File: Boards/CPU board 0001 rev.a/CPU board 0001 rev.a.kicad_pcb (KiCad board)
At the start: 2 copper layers, 165.9 x 187.4 mm, 78 parts, among them J1 CEC card edge connector large, U1 SPARE, U10 7432, U11 7442, U12 7406, U13 7406, U14 7442, U15 7442, U16 M8216, U17 M8216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

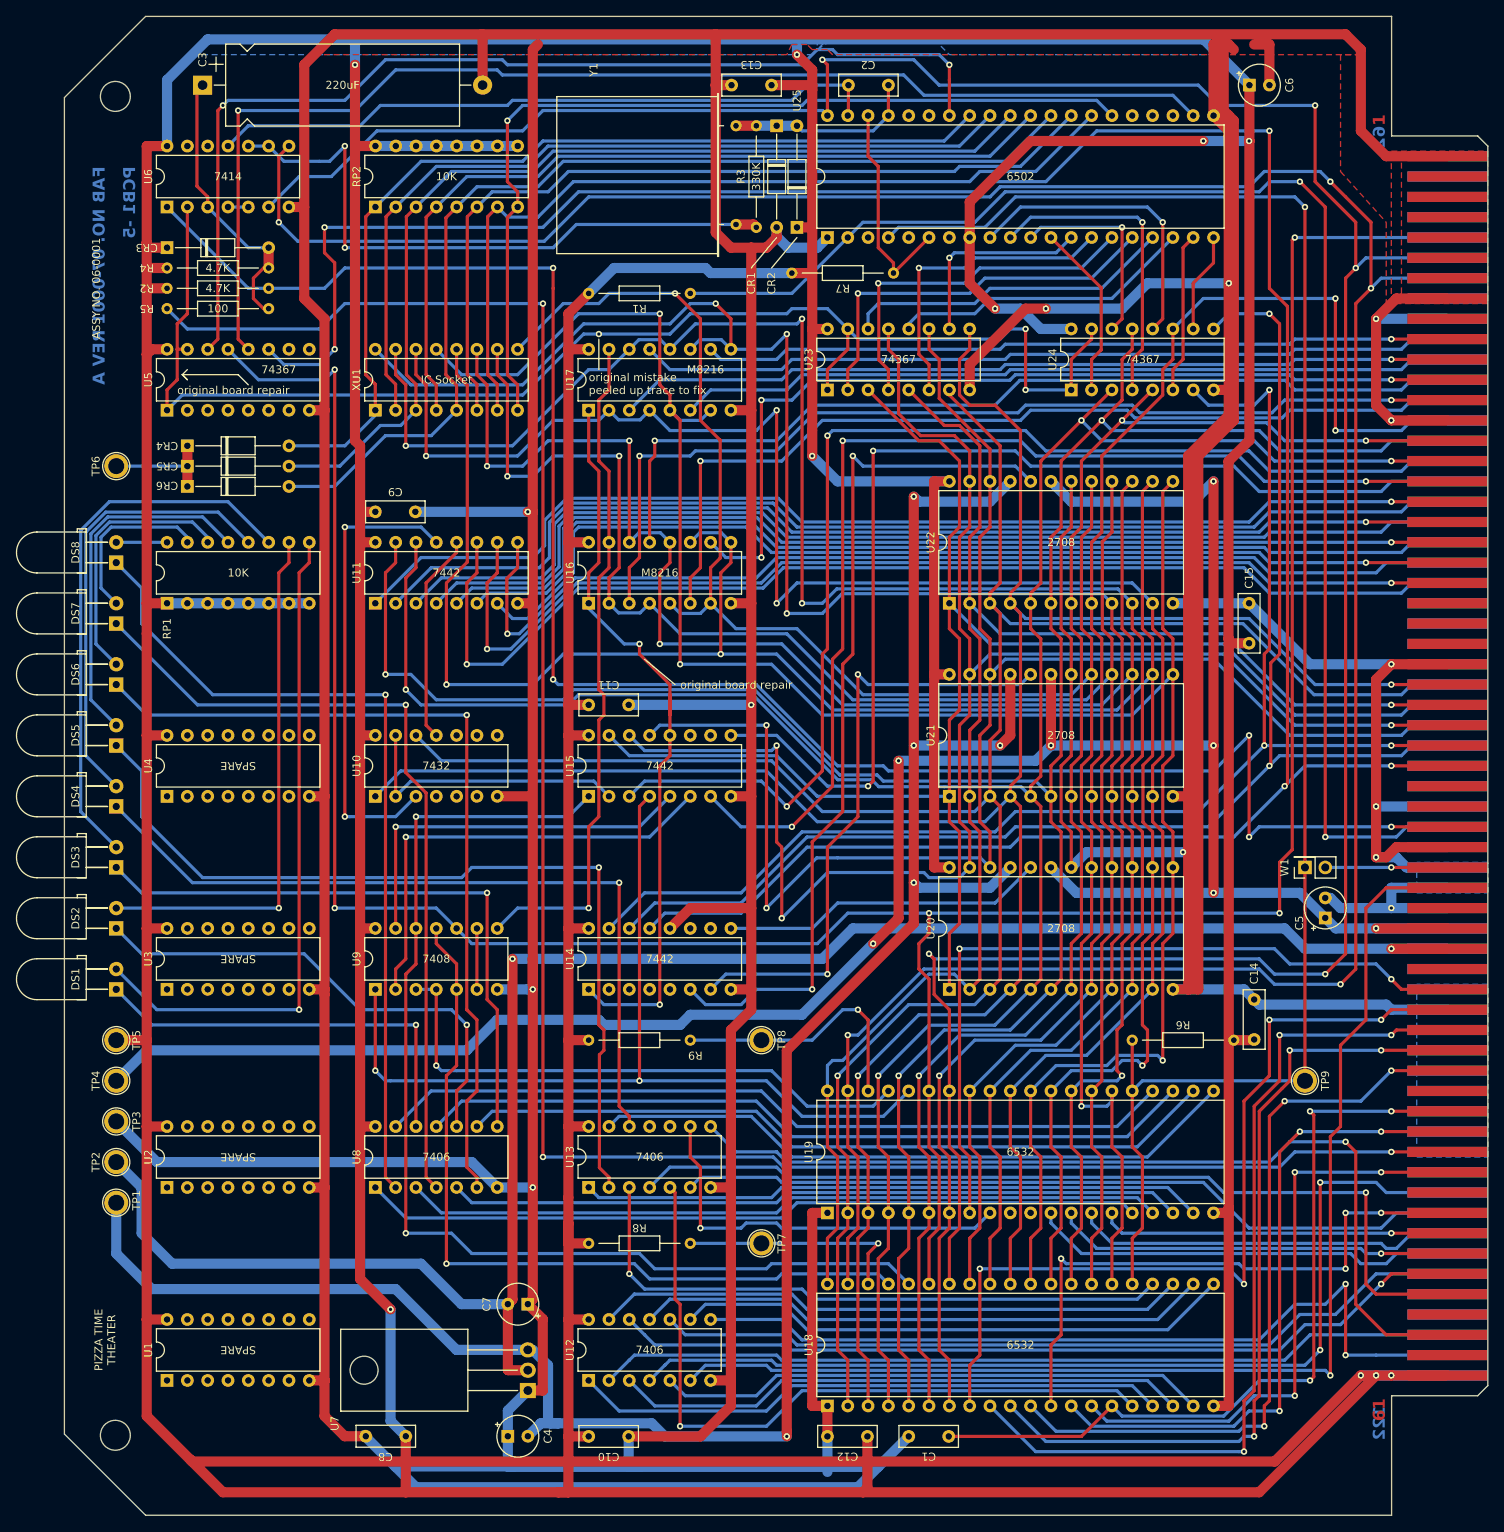
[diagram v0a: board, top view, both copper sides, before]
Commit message: updated boards per real one
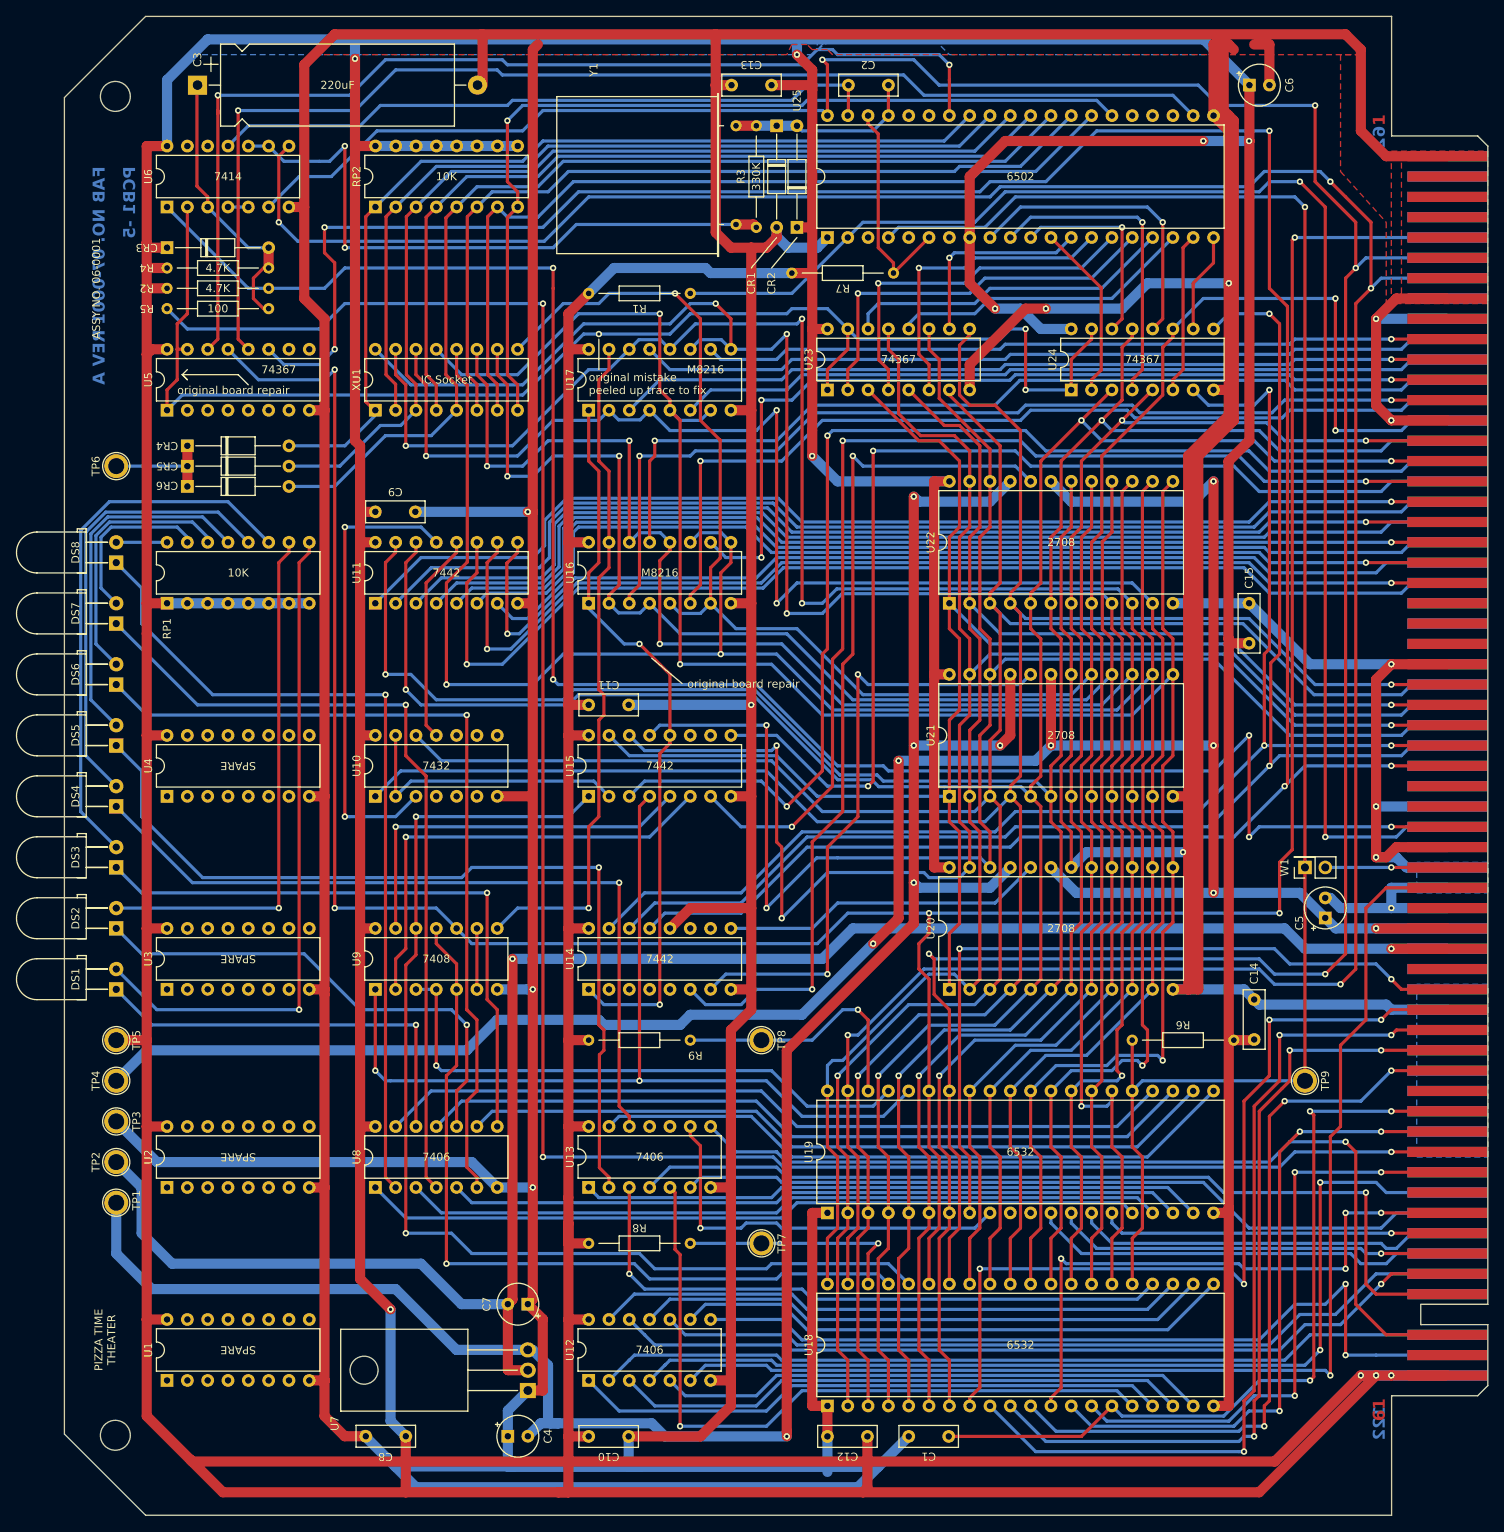
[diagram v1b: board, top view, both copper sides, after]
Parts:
- moved C3 0.63 mm to (58.4, 19.1)
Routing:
- net Net-(U14-0): track 93.4 -> 90.9 mm
- net +5V: track 1497.0 -> 1498.9 mm
- net cpu R/~{W}: track 132.6 -> 134.1 mm
- net Net-(CR3-A): track 35.8 -> 34.8 mm

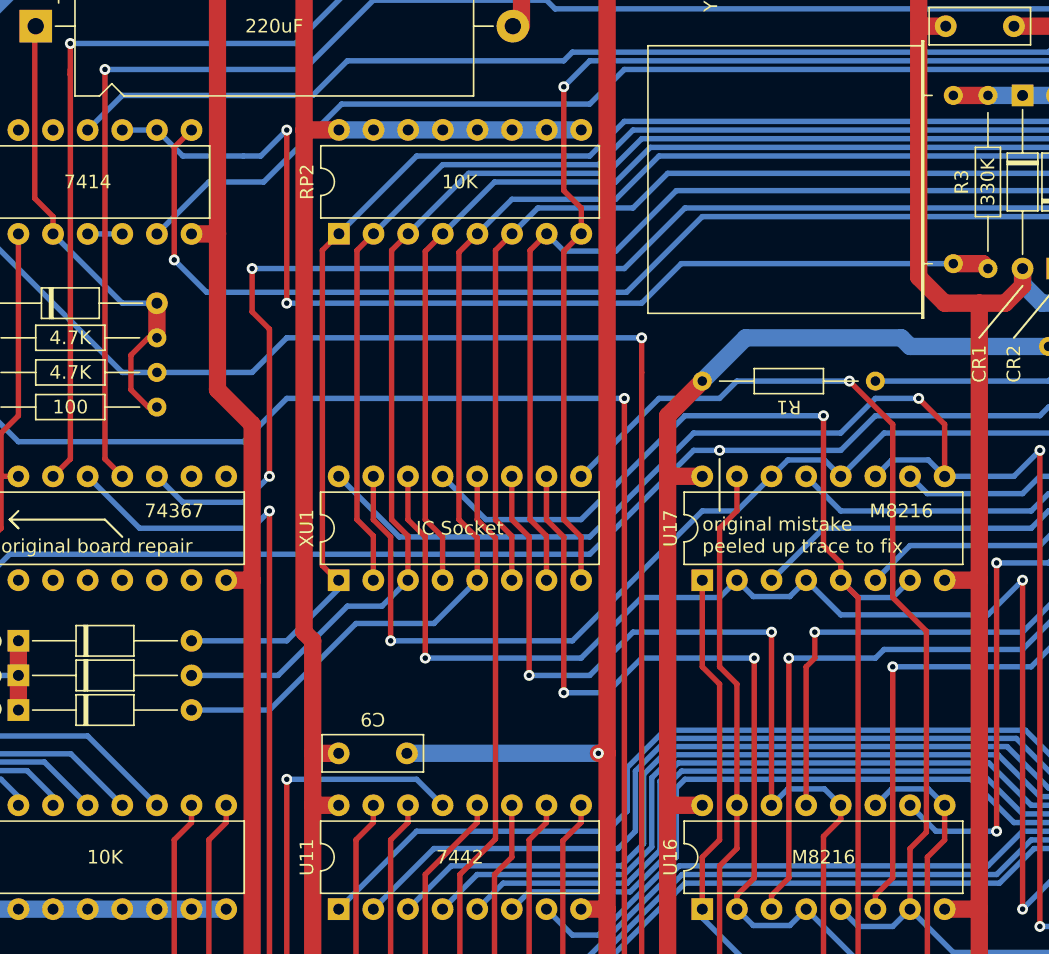
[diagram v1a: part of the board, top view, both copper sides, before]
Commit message: revisions from real life boards
tip130a is actually tip30a, widened holes for crystal, widened holes for big power resistor, fixed cpu board LED resistors
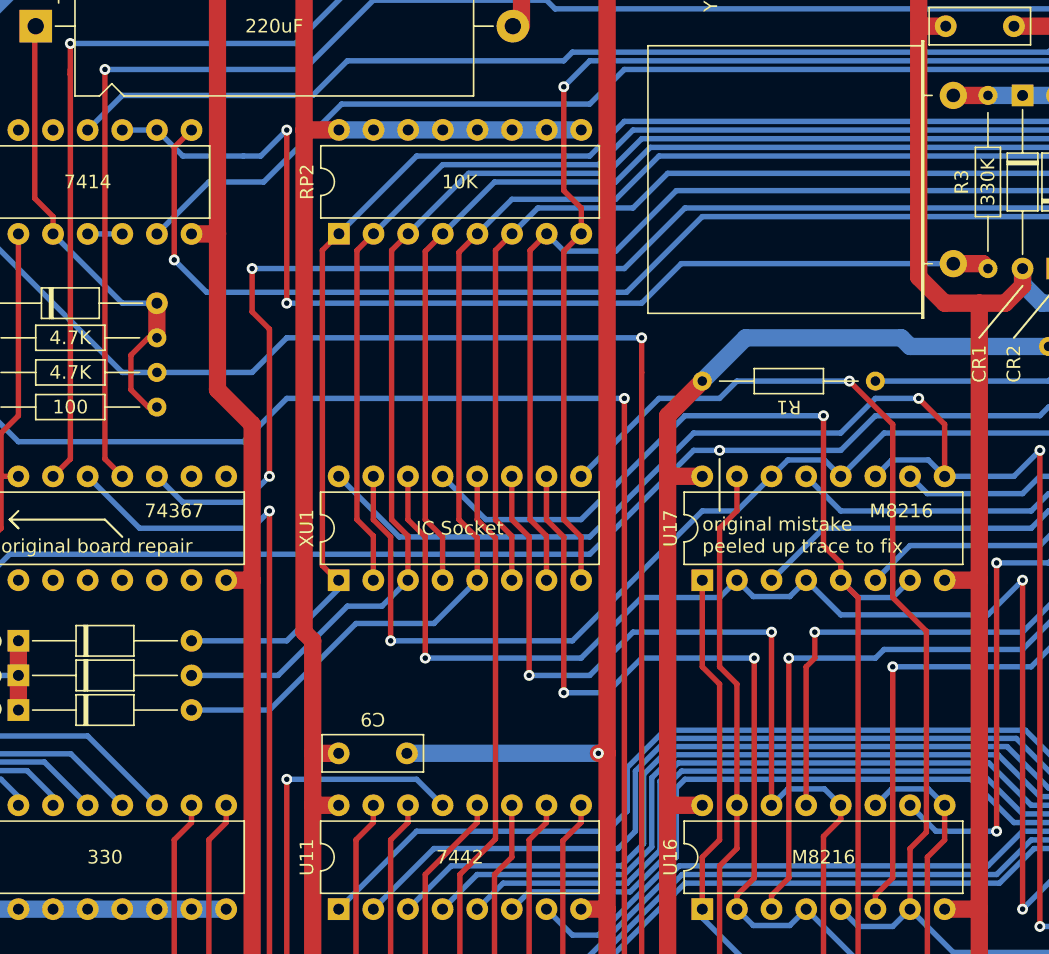
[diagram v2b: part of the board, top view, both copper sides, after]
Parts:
- RP1: value 10K -> 330
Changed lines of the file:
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@@
         (effects (font (size 1 1) (thickness 0.15)))
     )
-    (fp_text value "10K" (at 3.81 8.89 180) (layer "F.SilkS")
+    (fp_text value "330" (at 3.81 8.89 180) (layer "F.SilkS")
         (effects (font (size 1 1) (thickness 0.15)))
     )
@@
     (fp_line (start 16.135 2.5) (end -3.795 2.5)
       (stroke (width 0.1) (type solid)) (layer "F.Fab"))
-    (pad "1" thru_hole circle (at 0 0 270) (size 1.4 1.4) (drill 0.7) (layers "*.Cu" "*.Mask")
+    (pad "1" thru_hole circle (at 0 0 270) (size 2 2) (drill 1) (layers "*.Cu" "*.Mask")
       (net 8 "Net-(CR1-K)") (pinfunction "1") (pintype "passive"))
-    (pad "2" thru_hole circle (at 12.34 0 270) (size 1.4 1.4) (drill 0.7) (layers "*.Cu" "*.Mask")
+    (pad "2" thru_hole circle (at 12.34 0 270) (size 2 2) (drill 1) (layers "*.Cu" "*.Mask")
       (net 114 "Net-(R3-Pad1)") (pinfunction "2") (pintype "passive"))
     (model "${KICAD6_3DMODEL_DIR}/Crystal.3dshapes/Crystal_HC33-U_Horizontal.wrl"
